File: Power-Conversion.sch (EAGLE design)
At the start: 55 parts, among them J1 AVR_SPI_PRG_6PTH, U1 ATMEGA328P_TQFP, U2 LM1085IS-3.3

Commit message: stuffs
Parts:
- added F4: (no value), MotherboardParts:KEYSTONE_FUSE_3587
- added I2C_ESC11, I2C_ESC12: (no value), SparkFun-Connectors:M01PTH
- added V+_CONN, V+_ESC11, V+_ESC12, V-_CONN, V-_ESC11, V-_ESC12: (no value), SparkFun-Connectors:BANANA_CONN
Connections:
- new net N$2: I2C_ESC11.1, U$8.OUT10
- new net N$4: I2C_ESC12.1, U$8.OUT11
- new net N$6: F4.P$2, V+_ESC11.1, V+_ESC12.1
- net GND: now also V-_ESC11.1, V-_ESC12.1
- net V+: now also V+_CONN.1
- net V-: now also V-_CONN.1
- net VCC: now also F4.P$1
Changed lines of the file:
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@@
 <part name="C3" library="SparkFun-Capacitors" deviceset="0.1UF-25V(+80/-20%)(0603)" device="" value="0.1uF"/>
 <part name="GND16" library="supply1" deviceset="GND" device=""/>
+<part name="I2C_ESC11" library="SparkFun-Connectors" deviceset="M01" device="PTH"/>
+<part name="I2C_ESC12" library="SparkFun-Connectors" deviceset="M01" device="PTH"/>
+<part name="F4" library="MotherboardParts" deviceset="KEYSTONE_FUSE_3587" device=""/>
+<part name="V+_ESC11" library="SparkFun-Connectors" deviceset="BANANA_CONN" device=""/>
+<part name="V-_ESC11" library="SparkFun-Connectors" deviceset="BANANA_CONN" device=""/>
+<part name="GND19" library="supply1" deviceset="GND" device=""/>
+<part name="P+18" library="supply1" deviceset="VCC" device=""/>
+<part name="V+_ESC12" library="SparkFun-Connectors" deviceset="BANANA_CONN" device=""/>
+<part name="V-_ESC12" library="SparkFun-Connectors" deviceset="BANANA_CONN" device=""/>
+<part name="GND20" library="supply1" deviceset="GND" device=""/>
+<part name="V+_CONN" library="SparkFun-Connectors" deviceset="BANANA_CONN" device=""/>
+<part name="V-_CONN" library="SparkFun-Connectors" deviceset="BANANA_CONN" device=""/>
+<part name="P+19" library="supply1" deviceset="V+" device=""/>
+<part name="P-7" library="supply1" deviceset="V-" device=""/>
 </parts>
 <sheets>
@@
 <instance part="C3" gate="G$1" x="474.98" y="106.68"/>
 <instance part="GND16" gate="1" x="396.24" y="81.28" rot="MR0"/>
+<instance part="I2C_ESC11" gate="G$1" x="467.36" y="53.34" rot="MR0"/>
+<instance part="I2C_ESC12" gate="G$1" x="480.06" y="58.42" rot="MR0"/>
+<instance part="F4" gate="G$1" x="167.64" y="-25.4"/>
+<instance part="V+_ESC11" gate="G$1" x="185.42" y="-25.4"/>
+<instance part="V-_ESC11" gate="G$1" x="185.42" y="-30.48"/>
+<instance part="GND19" gate="1" x="182.88" y="-33.02"/>
+<instance part="P+18" gate="VCC" x="162.56" y="-22.86"/>
+<instance part="V+_ESC12" gate="G$1" x="185.42" y="-40.64"/>
+<instance part="V-_ESC12" gate="G$1" x="185.42" y="-45.72"/>
+<instance part="GND20" gate="1" x="182.88" y="-48.26"/>
+<instance part="V+_CONN" gate="G$1" x="45.72" y="76.2" rot="R180"/>
+<instance part="V-_CONN" gate="G$1" x="45.72" y="71.12" rot="R180"/>
+<instance part="P+19" gate="1" x="55.88" y="78.74"/>
+<instance part="P-7" gate="1" x="55.88" y="68.58"/>
 </instances>
 <busses>
@@
 <pinref part="P+15" gate="1" pin="V+"/>
 </segment>
+<segment>
+<pinref part="V+_CONN" gate="G$1" pin="1"/>
+<pinref part="P+19" gate="1" pin="V+"/>
+<wire x1="55.88" y1="76.2" x2="48.26" y2="76.2" width="0.1524" layer="91"/>
+</segment>
 </net>
 <net name="V-" class="0">
@@
 <pinref part="P-6" gate="1" pin="V-"/>
 </segment>
+<segment>
+<pinref part="V-_CONN" gate="G$1" pin="1"/>
+<pinref part="P-7" gate="1" pin="V-"/>
+<wire x1="55.88" y1="71.12" x2="48.26" y2="71.12" width="0.1524" layer="91"/>
+</segment>
 </net>
 <net name="VCC" class="0">
@@
 <pinref part="U2" gate="A" pin="IN"/>
 <pinref part="P+10" gate="VCC" pin="VCC"/>
+</segment>
+<segment>
+<pinref part="F4" gate="G$1" pin="P$1"/>
+<pinref part="P+18" gate="VCC" pin="VCC"/>
 </segment>
 </net>
@@
 <pinref part="GND16" gate="1" pin="GND"/>
 <junction x="396.24" y="83.82"/>
+</segment>
+<segment>
+<pinref part="V-_ESC11" gate="G$1" pin="1"/>
+<pinref part="GND19" gate="1" pin="GND"/>
+</segment>
+<segment>
+<pinref part="V-_ESC12" gate="G$1" pin="1"/>
+<pinref part="GND20" gate="1" pin="GND"/>
 </segment>
 </net>
@@
 </segment>
 </net>
+<net name="N$2" class="0">
+<segment>
+<pinref part="U$8" gate="G$1" pin="OUT10"/>
+<pinref part="I2C_ESC11" gate="G$1" pin="1"/>
+<wire x1="452.12" y1="53.34" x2="459.74" y2="53.34" width="0.1524" layer="91"/>
+</segment>
+</net>
+<net name="N$4" class="0">
+<segment>
+<pinref part="U$8" gate="G$1" pin="OUT11"/>
+<pinref part="I2C_ESC12" gate="G$1" pin="1"/>
+<wire x1="452.12" y1="58.42" x2="472.44" y2="58.42" width="0.1524" layer="91"/>
+</segment>
+</net>
+<net name="N$6" class="0">
+<segment>
+<pinref part="V+_ESC11" gate="G$1" pin="1"/>
+<pinref part="F4" gate="G$1" pin="P$2"/>
+<wire x1="172.72" y1="-25.4" x2="175.26" y2="-25.4" width="0.1524" layer="91"/>
+<pinref part="V+_ESC12" gate="G$1" pin="1"/>
+<wire x1="175.26" y1="-25.4" x2="182.88" y2="-25.4" width="0.1524" layer="91"/>
+<wire x1="175.26" y1="-25.4" x2="175.26" y2="-40.64" width="0.1524" layer="91"/>
+<wire x1="175.26" y1="-40.64" x2="182.88" y2="-40.64" width="0.1524" layer="91"/>
+<junction x="175.26" y="-25.4"/>
+</segment>
+</net>

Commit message: Fuse
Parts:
- renumbered I2C_ESC1 to PWM_ESC1, I2C_ESC10 to PWM_ESC10, I2C_ESC11 to PWM_ESC11, I2C_ESC12 to PWM_ESC12, I2C_ESC2 to PWM_ESC2, I2C_ESC3 to PWM_ESC3, I2C_ESC4 to PWM_ESC4, I2C_ESC5 to PWM_ESC5, I2C_ESC6 to PWM_ESC6, I2C_ESC7 to PWM_ESC7, I2C_ESC8 to PWM_ESC8, I2C_ESC9 to PWM_ESC9

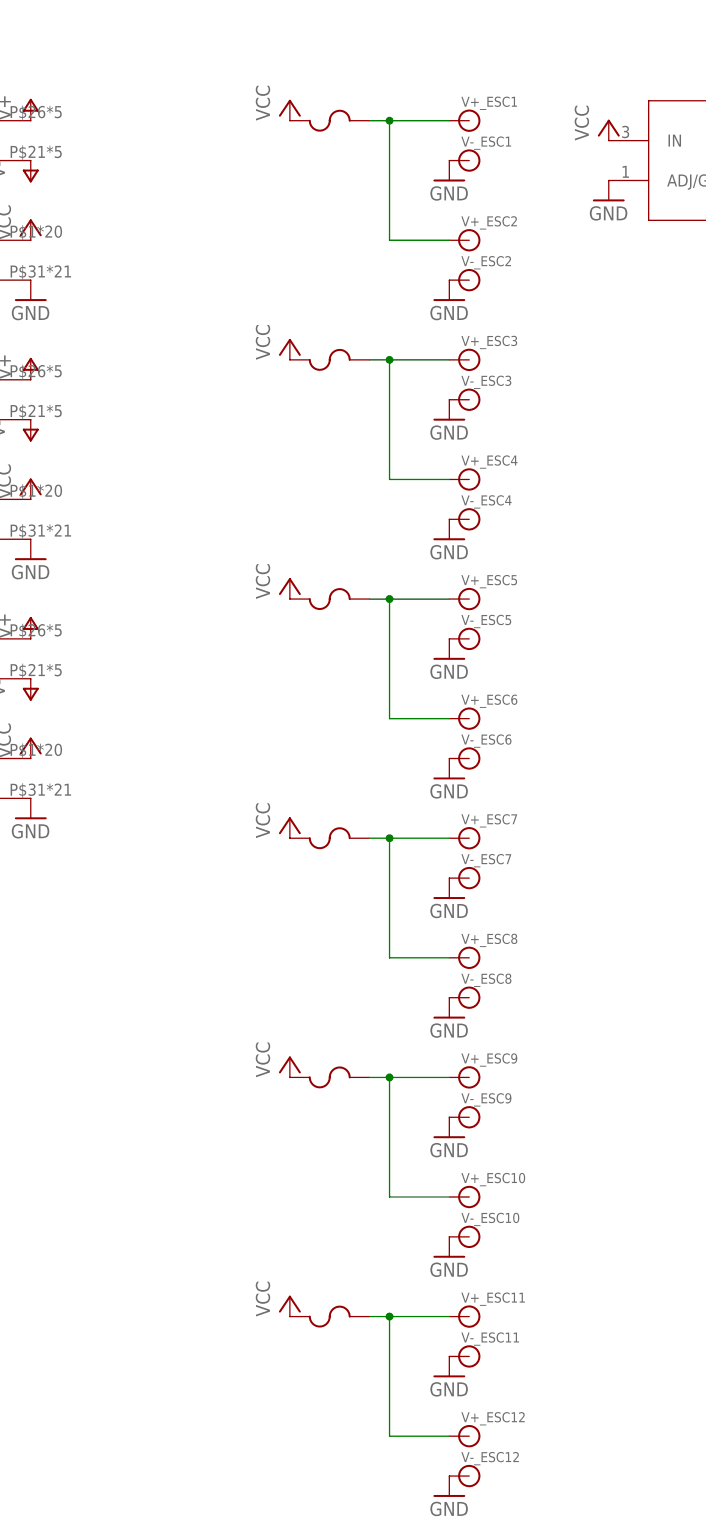
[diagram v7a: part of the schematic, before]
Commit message: Replaced normal fuses with individual PTC fuses
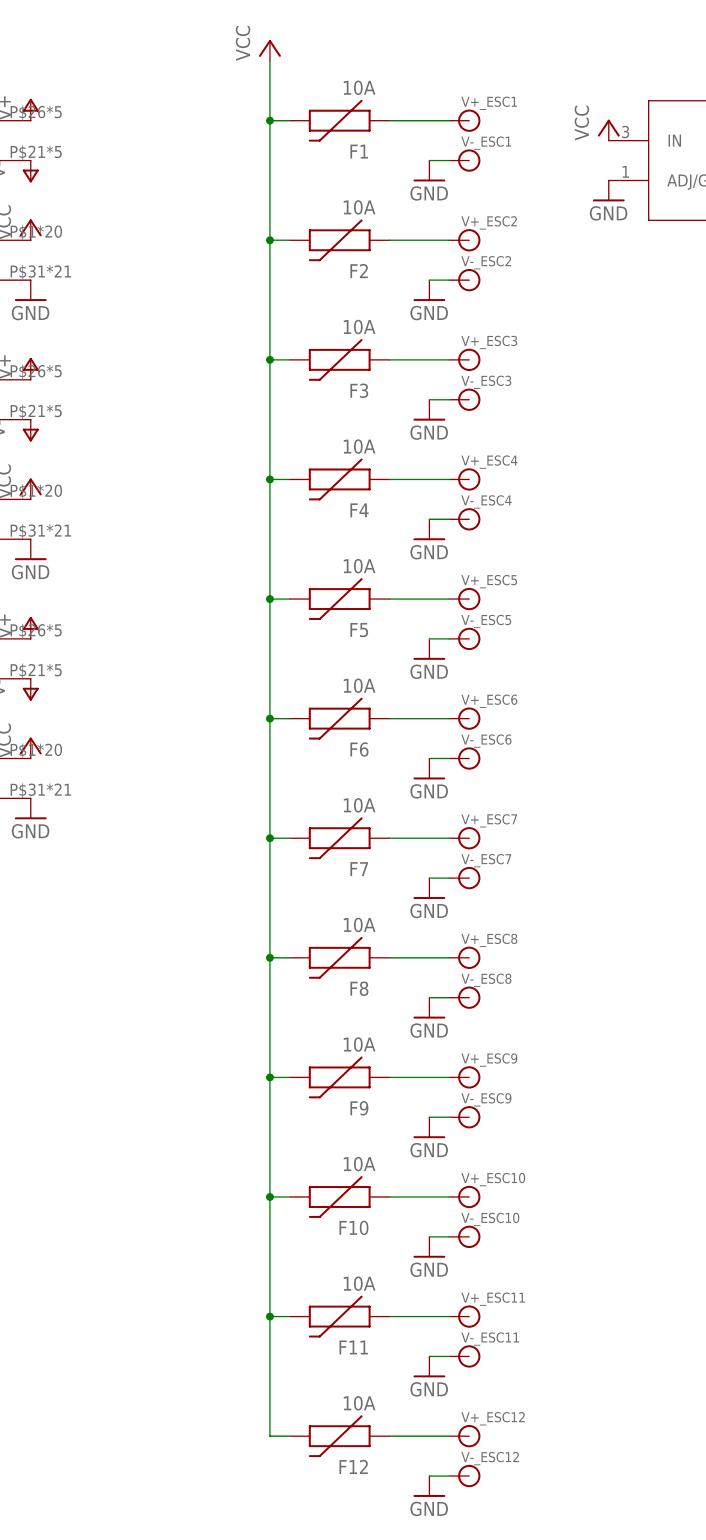
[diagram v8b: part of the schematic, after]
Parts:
- added F10, F11, F12, F6, F8, F9: 10A, PowerComponents:PTC(2920L)
- F1, F2, F3, F4, F5, F7: value (none) -> 10A; device MotherboardParts:KEYSTONE_FUSE_3587 -> PowerComponents:PTC(2920L)
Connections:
- new net N$28: F9.1, V+_ESC9.1
- new net N$30: F10.1, V+_ESC10.1
- new net N$32: F4.1, V+_ESC4.1
- new net N$33: F11.1, V+_ESC11.1
- new net N$34: F12.1, V+_ESC12.1
- new net N$8: F7.1, V+_ESC7.1
- net N$1: now also F1.1; no longer F1.P$2, V+_ESC2.1
- net N$11: now also F8.1, V+_ESC8.1; no longer F2.P$2, V+_ESC10.1, V+_ESC9.1
- net N$3: now also F2.1, V+_ESC2.1; no longer F3.P$2, V+_ESC3.1, V+_ESC4.1
- net N$5: now also F3.1, V+_ESC3.1; no longer F5.P$2, V+_ESC5.1, V+_ESC6.1
- net N$6: now also F5.1, V+_ESC5.1; no longer F4.P$2, V+_ESC11.1, V+_ESC12.1
- net N$7: now also F6.1, V+_ESC6.1; no longer F7.P$2, V+_ESC7.1, V+_ESC8.1
- net VCC: now also F1.2, F10.2, F11.2, F12.2, F2.2, F3.2, F4.2, F5.2, F6.2, F7.2, F8.2, F9.2; no longer F1.P$1, F2.P$1, F3.P$1, F4.P$1, F5.P$1, F7.P$1
